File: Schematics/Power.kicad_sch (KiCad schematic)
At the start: 0 parts

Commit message: [WIP SiC Single Phase Inverter]
- Added AC - DC converter for 15V isolated supply
- Added 2x IRM-05 to the power sub sheet
- Added 3D part for the IRM-05
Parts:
- added PS1, PS2: IRM-03-15, SiC_Inverter:IRM-03-15, symbol SiC_Inverter:IRM-03-15
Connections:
- new net +15V_ISO_LALS: PS1.16 (+VO)
- new net +15V_ISO_LBLS: PS2.16 (+VO)
- new net DC+_IN_1: PS1.1 (AC/L)
- new net DC+_IN_2: PS2.1 (AC/L)
- new net GND: PS1.3 (AC/N), PS2.3 (AC/N)
- new net GND_ISO_LAHS: PS1.14 (-VO)
- new net GND_ISO_LBHS: PS2.14 (-VO)

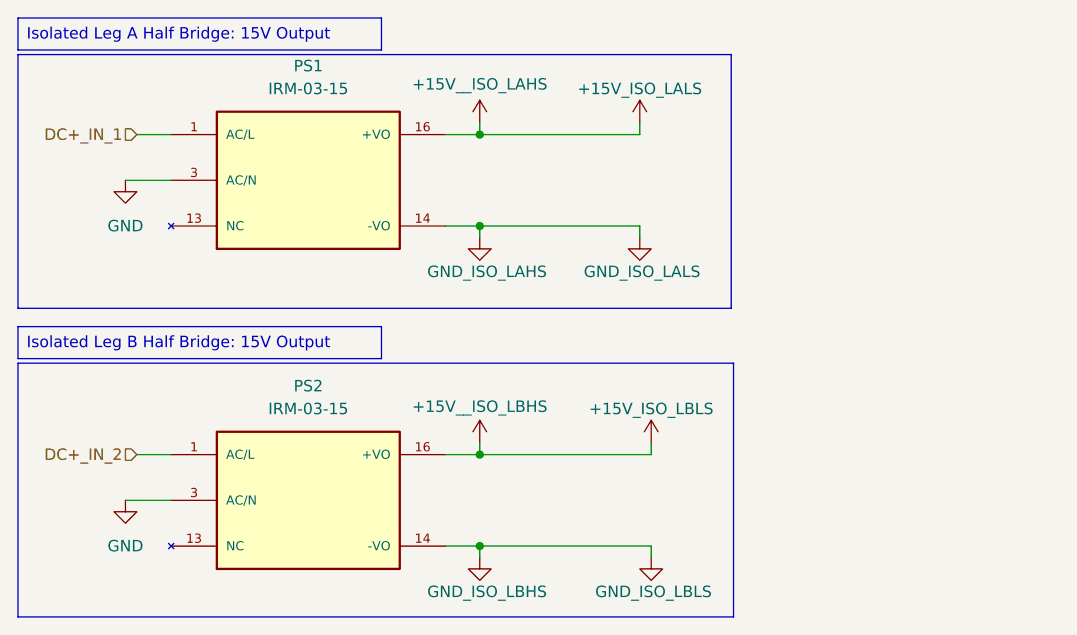
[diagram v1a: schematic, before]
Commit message: [WIP Single Phase SiC Inverter]
- Added molex 4 pin pcb connector for +15V power
- Added 3d model, symbol and footprint
- Added datasheet for molex connector
- Added Male and Female pcb - pcb connectors to all sub sheets
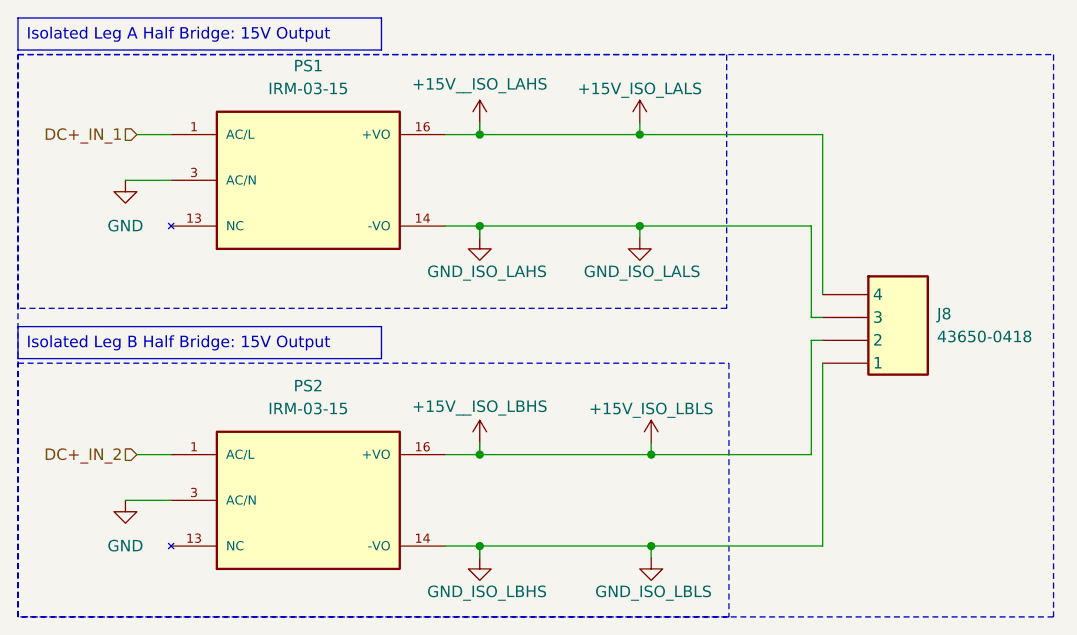
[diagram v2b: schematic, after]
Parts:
- added J8: 43650-0418, SiC_Inverter:436500418, symbol SiC_Inverter:43650-0418
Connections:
- net +15V_ISO_LALS: now also J8.4
- net +15V_ISO_LBLS: now also J8.2
- net GND_ISO_LAHS: now also J8.3
- net GND_ISO_LBHS: now also J8.1
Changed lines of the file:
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@@
 	(rectangle
 		(start 120.142 102.87)
-		(end 199.644 131.064)
-		(stroke
-			(width 0)
-			(type default)
+		(end 199.136 131.064)
+		(stroke
+			(width 0)
+			(type dash)
 		)
 		(fill
@@
 	(rectangle
 		(start 120.142 68.58)
-		(end 199.39 96.774)
-		(stroke
-			(width 0)
-			(type default)
+		(end 198.882 96.774)
+		(stroke
+			(width 0)
+			(type dash)
+		)
+		(fill
+			(type none)
+		)
+	)
+	(rectangle
+		(start 120.142 68.58)
+		(end 235.204 131.064)
+		(stroke
+			(width 0)
+			(type dash)
 		)
 		(fill
@@
 	)
 	(junction
+		(at 189.23 77.47)
+		(diameter 0)
+		(color 0 0 0 0)
+	)
+	(junction
+		(at 189.23 87.63)
+		(diameter 0)
+		(color 0 0 0 0)
+	)
+	(junction
+		(at 190.5 123.19)
+		(diameter 0)
+		(color 0 0 0 0)
+	)
+	(junction
 		(at 171.45 113.03)
 		(diameter 0)
@@
 		(color 0 0 0 0)
 	)
+	(junction
+		(at 190.5 113.03)
+		(diameter 0)
+		(color 0 0 0 0)
+	)
 	(wire
 		(pts
@@
 	(wire
 		(pts
+			(xy 209.55 123.19) (xy 190.5 123.19)
+		)
+		(stroke
+			(width 0)
+			(type default)
+		)
+	)
+	(wire
+		(pts
+			(xy 208.28 87.63) (xy 208.28 97.79)
+		)
+		(stroke
+			(width 0)
+			(type default)
+		)
+	)
+	(wire
+		(pts
+			(xy 209.55 102.87) (xy 209.55 123.19)
+		)
+		(stroke
+			(width 0)
+			(type default)
+		)
+	)
+	(wire
+		(pts
 			(xy 171.45 111.76) (xy 171.45 113.03)
 		)
@@
 	(wire
 		(pts
+			(xy 209.55 100.33) (xy 208.28 100.33)
+		)
+		(stroke
+			(width 0)
+			(type default)
+		)
+	)
+	(wire
+		(pts
+			(xy 189.23 77.47) (xy 209.55 77.47)
+		)
+		(stroke
+			(width 0)
+			(type default)
+		)
+	)
+	(wire
+		(pts
+			(xy 208.28 87.63) (xy 189.23 87.63)
+		)
+		(stroke
+			(width 0)
+			(type default)
+		)
+	)
+	(wire
+		(pts
 			(xy 132.08 118.11) (xy 137.16 118.11)
 		)
@@
 	(wire
 		(pts
+			(xy 208.28 113.03) (xy 190.5 113.03)
+		)
+		(stroke
+			(width 0)
+			(type default)
+		)
+	)
+	(wire
+		(pts
 			(xy 167.64 87.63) (xy 171.45 87.63)
 		)
@@
 	(wire
 		(pts
+			(xy 208.28 100.33) (xy 208.28 113.03)
+		)
+		(stroke
+			(width 0)
+			(type default)
+		)
+	)
+	(wire
+		(pts
+			(xy 209.55 95.25) (xy 209.55 77.47)
+		)
+		(stroke
+			(width 0)
+			(type default)
+		)
+	)
+	(wire
+		(pts
 			(xy 133.35 77.47) (xy 137.16 77.47)
+		)
+		(stroke
+			(width 0)
+			(type default)
+		)
+	)
+	(wire
+		(pts
+			(xy 209.55 97.79) (xy 208.28 97.79)
 		)
 		(stroke
@@
 					(unit 1)
 				)
+			)
+		)
+	)
+	(symbol
+		(lib_id "SiC_Inverter:43650-0418")
+		(at 209.55 92.71 0)
+		(unit 1)
+		(exclude_from_sim no)
+		(in_bom yes)
+		(on_board yes)
+		(dnp no)
+		(fields_autoplaced yes)
+		(property "Reference" "J8"
+			(at 222.25 97.4089 0)
+			(effects
+				(font
+					(size 1.27 1.27)
+				)
+				(justify left)
+			)
+		)
+		(property "Value" "43650-0418"
+			(at 222.25 99.9489 0)
+			(effects
+				(font
+					(size 1.27 1.27)
+				)
+				(justify left)
+			)
+		)
+		(property "Footprint" "SiC_Inverter:436500418"
+			(at 226.06 187.63 0)
+			(effects
+				(font
+					(size 1.27 1.27)
+				)
+				(justify left top)
+				(hide yes)
+			)
+		)
+		(property "Datasheet" "https://www.molex.com/pdm_docs/sd/436500218_sd.pdf"
+			(at 226.06 287.63 0)
+			(effects
+				(font
+					(size 1.27 1.27)
+				)
+				(justify left top)
+				(hide yes)
+			)
+		)
+		(property "Description" "Micro-Fit 3.0 Vertical Header, 3.00mm Pitch, Single Row, 4 Circuits, with PCB Press-fit Metal Retention Clip, Glow-Wire Capable, Black"
+			(at 273.558 111.506 0)
+			(effects
+				(font
+					(size 1.27 1.27)
+				)
+				(hide yes)
+			)
+		)
+		(property "Mouser Part Number" "538-43650-0418"
+			(at 226.06 587.63 0)
+			(effects
+				(font
+					(size 1.27 1.27)
+				)
+				(justify left top)
+				(hide yes)
+			)
+		)
+		(property "Manufacturer_Name" "Molex"
+			(at 226.06 787.63 0)
+			(effects
+				(font
+					(size 1.27 1.27)
+				)
+				(justify left top)
+				(hide yes)
+			)
+		)
+		(property "Manufacturer_Part_Number" "43650-0418"
+			(at 226.06 887.63 0)
+			(effects
+				(font
+					(size 1.27 1.27)
+				)
+				(justify left top)
+				(hide yes)
+			)
+		)
+		(pin "3"
+		)
+		(pin "4"
+		)
+		(pin "2"
+		)
+		(pin "1"
+		)
+		(instances
+			(project ""
+				(path "/a1ed0539-9735-4ad1-a8fd-87e26e7fce16/e9f9d5ca-7f9f-4dc3-b303-71fca817b963"
+					(reference "J8")
+					(unit 1)
+				)

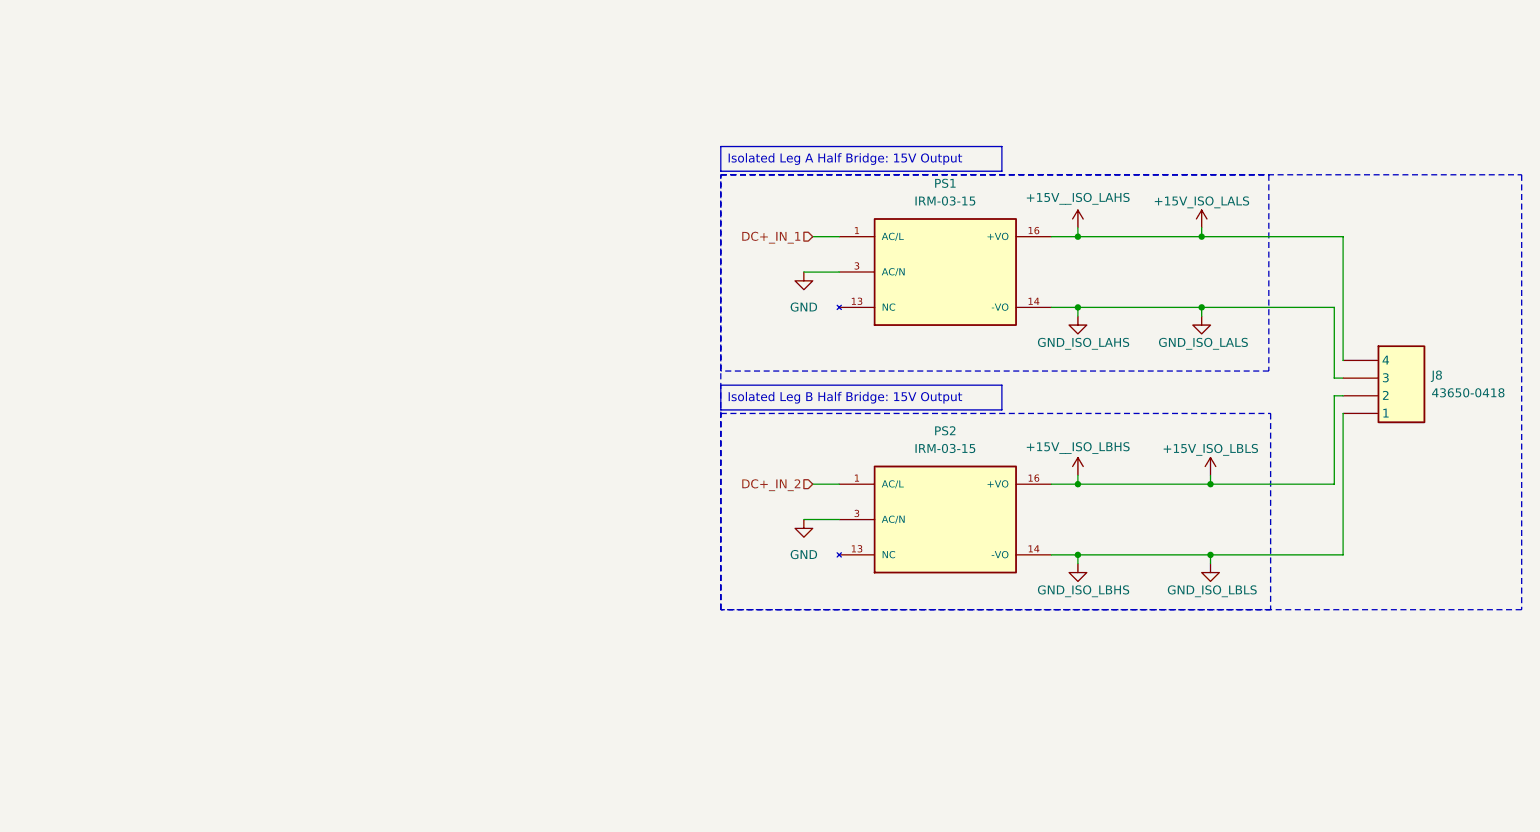
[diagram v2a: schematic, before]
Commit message: [WIP SiC Single Phase Inverter]
- Updated README to have a Block Diagram
- WIP Sub sheets Power, Controller
- Added the F2800 controller to the project
- Added the controller to the controller sub sheet
- Added text for a 15V to 3V3 voltage converter
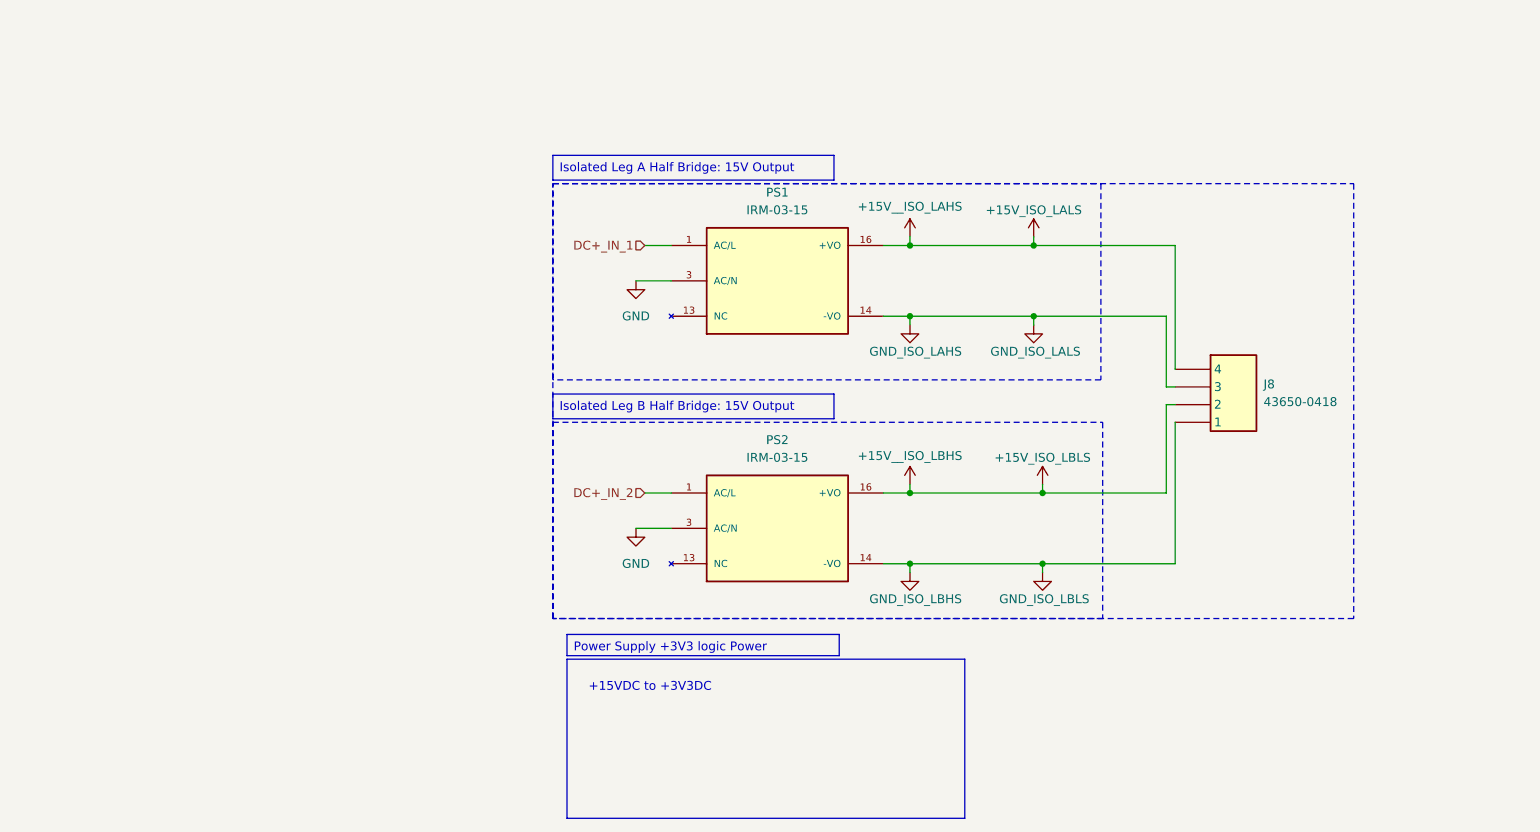
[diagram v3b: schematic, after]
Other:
- note added: "+15VDC to +3V3DC"
- moved on the sheet: J8, PS1, PS2

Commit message: [WIP Single Phase Inverter]
- Changed all Refs within each sub sheet (Stripe)
- Added 3V3 Power Supply off of 15V iso supply
- Added footprint, symbol and 3d part
- updated PCB with new part
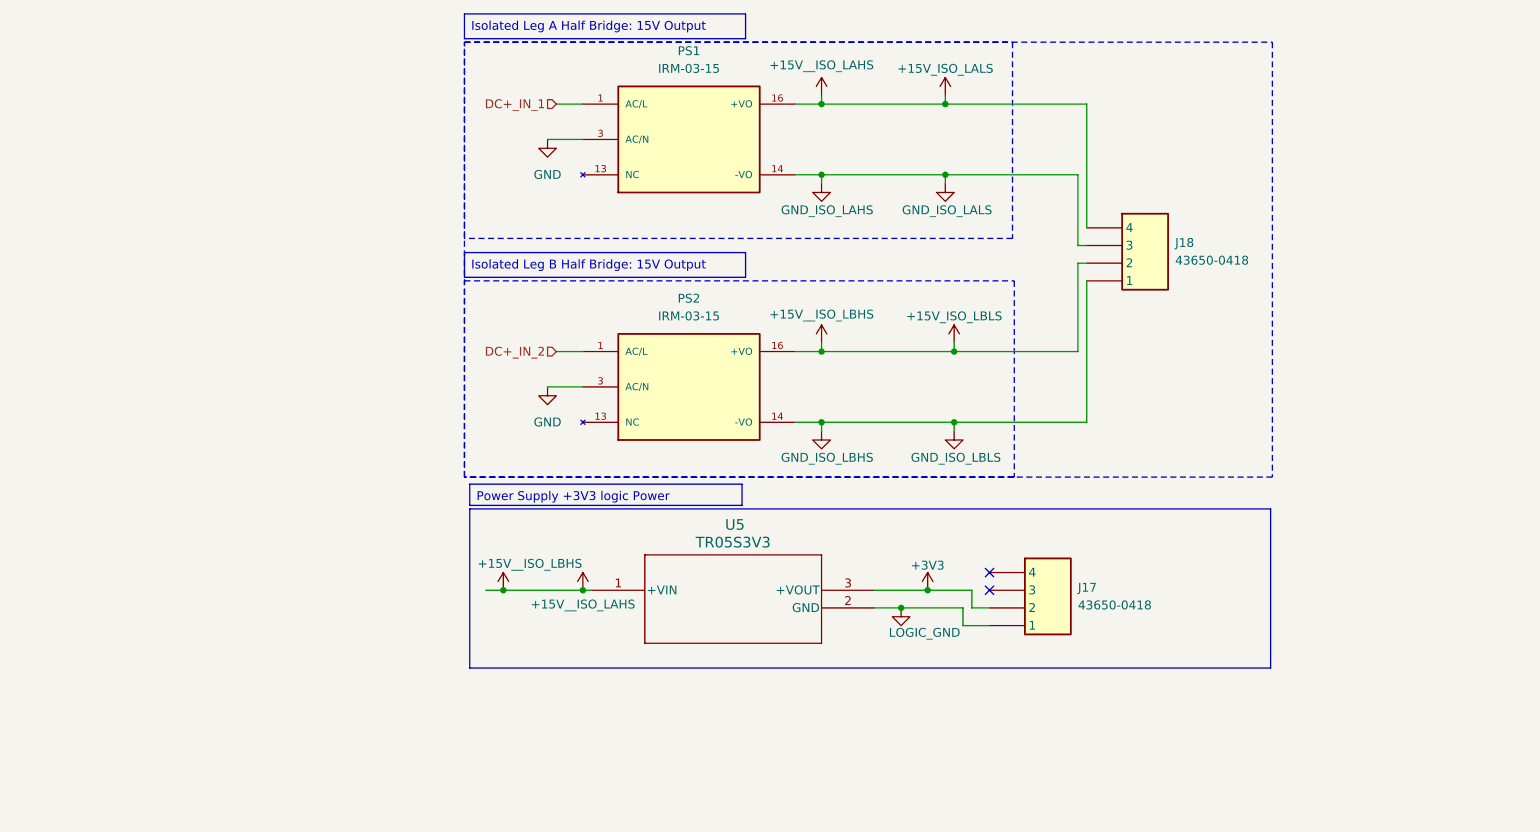
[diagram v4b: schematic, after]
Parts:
- added J17: 43650-0418, SiC_Inverter:436500418, symbol SiC_Inverter:43650-0418
- added U5: TR05S3V3, SiC_Inverter:TR05S3V3, symbol SiC_Inverter:TR05S3V3
- renumbered J8 to J18
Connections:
- net +15V_ISO_LBLS is gone; now on net +15V_ISO_LALS: J18.2, PS2.16 (+VO)
- net +15V_ISO_LALS: now also U5.1 (+VIN)
- new net +3V3: J17.2, U5.3 (+VOUT)
- new net LOGIC_GND: J17.1, U5.2 (GND)
- no-connect marks 0 -> 2
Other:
- note removed: "+15VDC to +3V3DC"
- moved on the sheet: J18, PS1, PS2

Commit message: [Milestone Compelted Controller and USB]
- Added Test Points
- Completed USB circuit to Controller
- Wired up Controller
- Added Connectors to Power Subsheet and 12pin from cotnroller to Full
  Bridge
- Added 3d models for USB compoents
- General fixes to subsheets
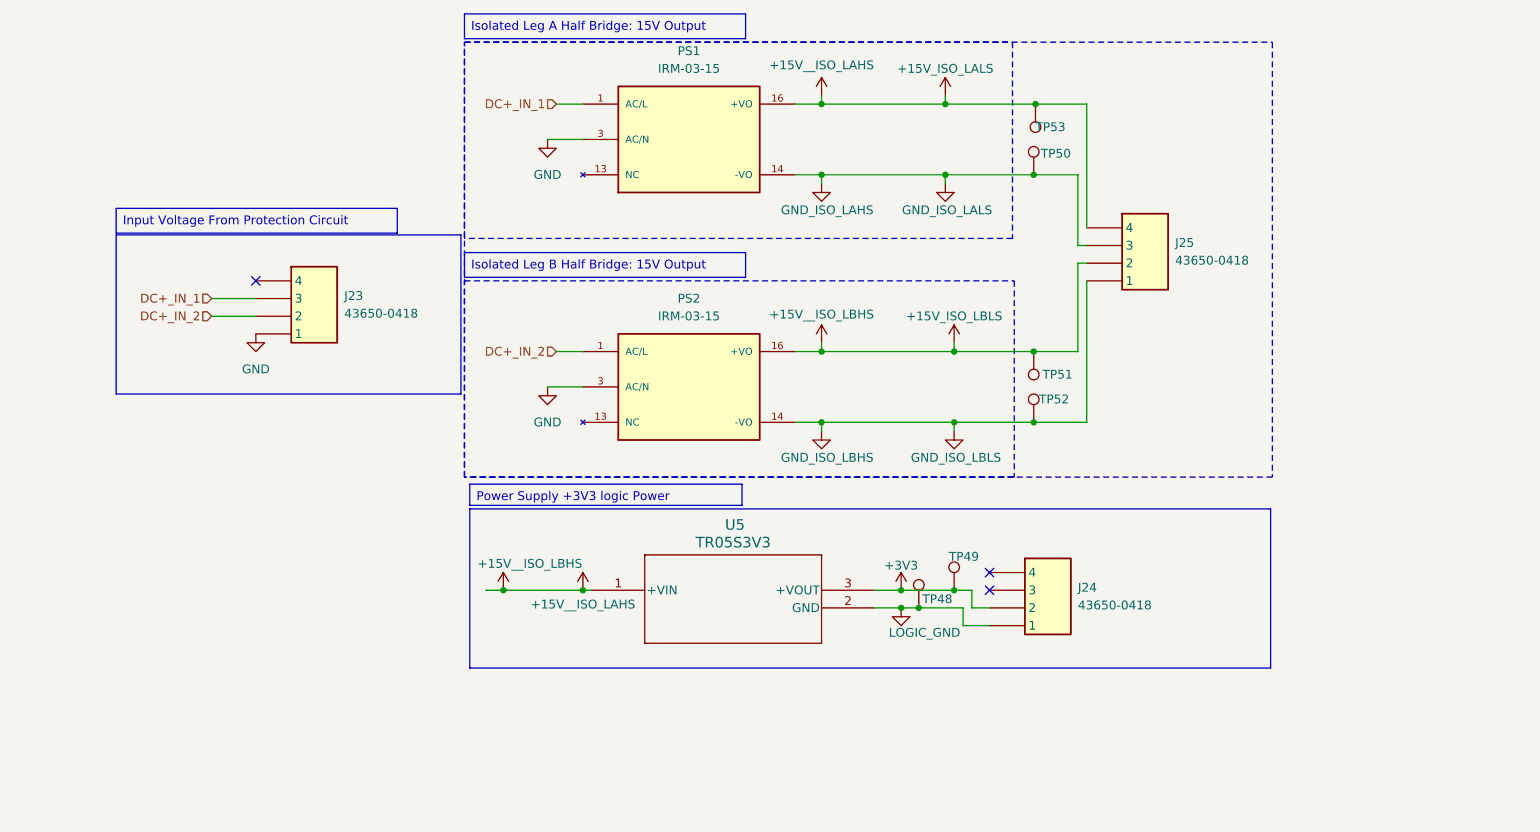
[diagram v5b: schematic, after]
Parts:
- added J23: 43650-0418, SiC_Inverter:436500418, symbol SiC_Inverter:43650-0418
- added TP48, TP50, TP52: 5281, SiC_Inverter:5281, symbol SiC_Inverter:5281
- added TP49, TP51, TP53: 5277, SiC_Inverter:5277, symbol SiC_Inverter:5277
- renumbered J17 to J24, J18 to J25
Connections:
- net +15V_ISO_LALS: now also TP51.1, TP53.1
- net +3V3: now also TP49.1
- net DC+_IN_1: now also J23.3
- net DC+_IN_2: now also J23.2
- net GND: now also J23.1
- net GND_ISO_LAHS: now also TP50.1
- net GND_ISO_LBHS: now also TP52.1
- net LOGIC_GND: now also TP48.1
- no-connect marks 2 -> 3
